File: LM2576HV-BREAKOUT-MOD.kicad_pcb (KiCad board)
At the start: 2 copper layers, 39 x 34 mm, 16 parts, among them J1 Conn_01x01, J2 Conn_01x01, J3 Conn_01x01, J4 Conn_01x01, U1 LM2576HVS-ADJ

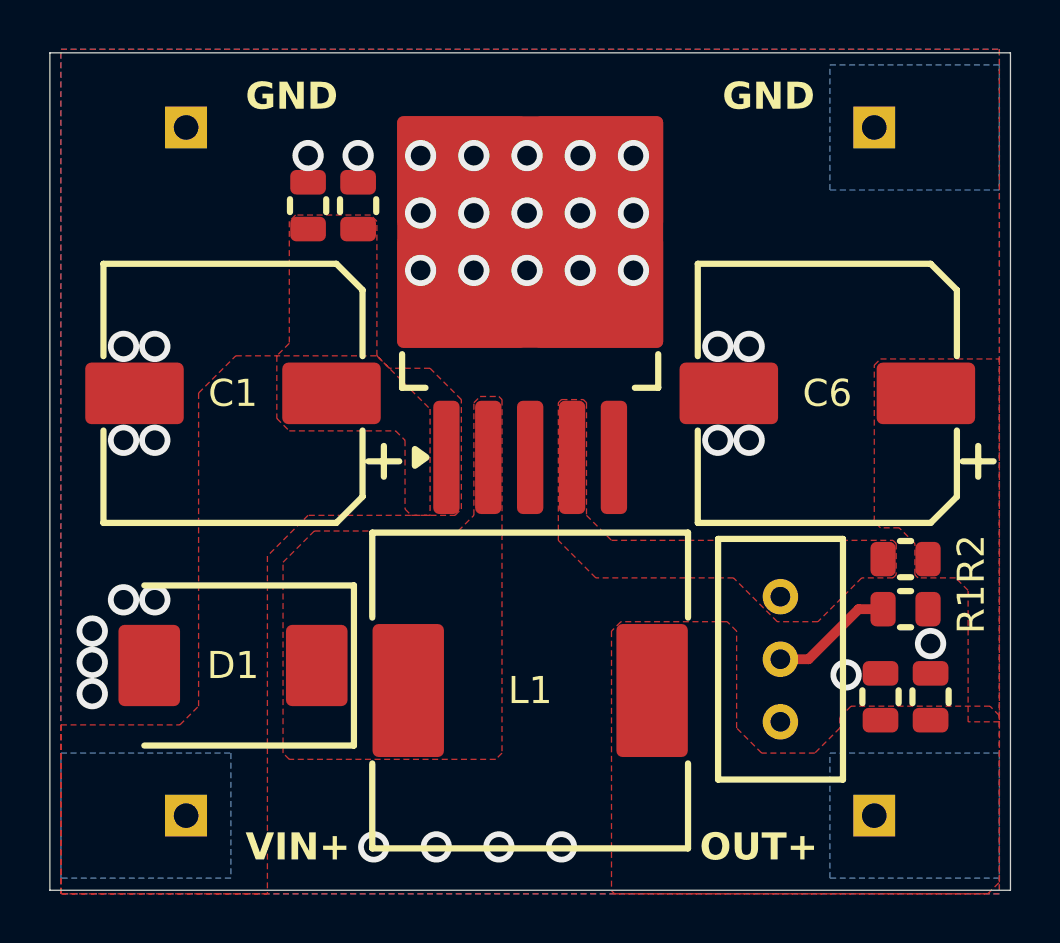
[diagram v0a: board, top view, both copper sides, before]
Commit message: Update LM2576HV Breakout Mod to use LM2576HVS-12
- Removed unused potentiometer symbol and associated properties from schematic.
- Updated LM2576HVS-ADJ references to LM2576HVS-12 in schematic, including properties and symbols.
- Adjusted junction and wire positions for better layout.
- Removed redundant wires and no-connects to clean up the schematic.
- Updated connector positions for better alignment.
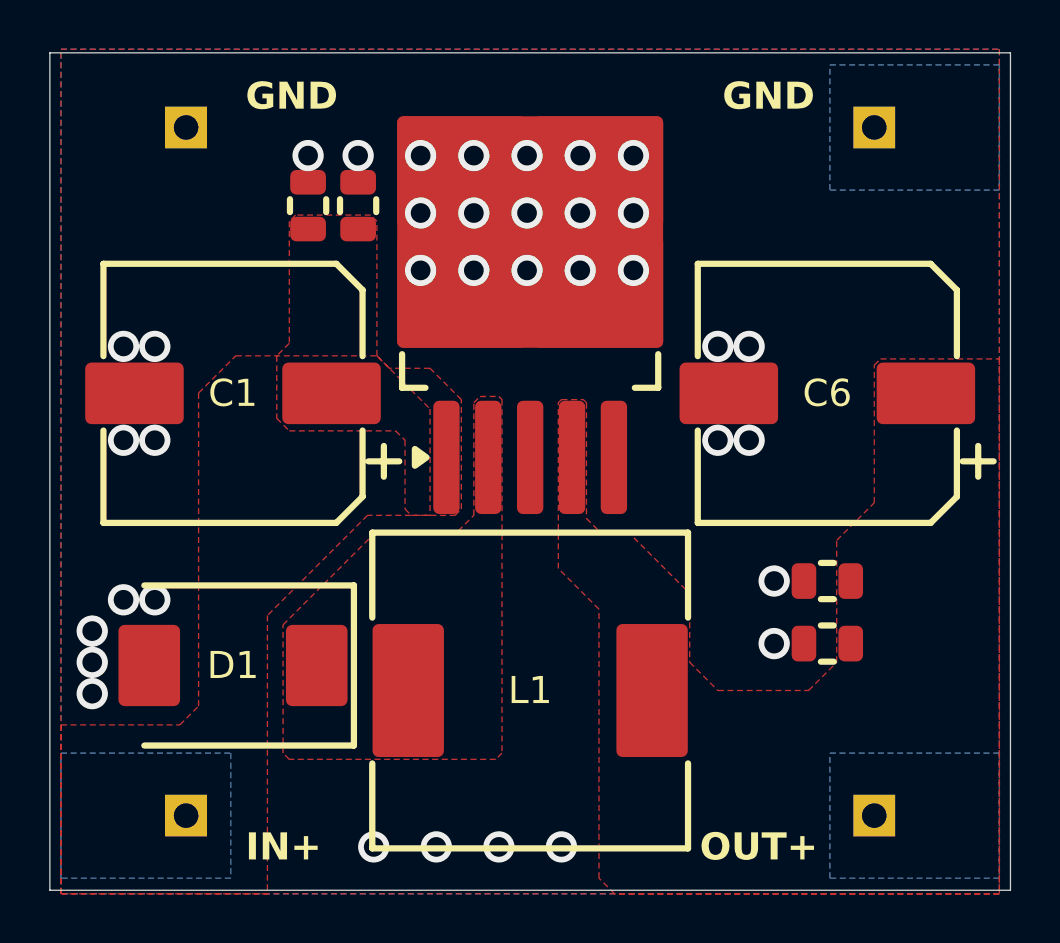
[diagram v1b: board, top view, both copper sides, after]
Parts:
- removed R1: 1k, Resistor_SMD:R_0805_2012Metric
- removed R2: 1k5, Resistor_SMD:R_0805_2012Metric
- removed RV1: 10k, Potentiometer_THT:Potentiometer_Bourns_3296W_Vertical
- U1: value LM2576HVS-ADJ -> LM2576HVS-12
- moved C4 6.30 mm to (177.2, 81.9), turned to 180 degrees
- moved C5 3.05 mm to (177.2, 84.5), turned to 180 degrees
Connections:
- U1 pad 4: FB -> VOUT
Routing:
- net /TRIM: track 5.01 -> 0.00 mm
- removed copper zone on F.Cu, net FB
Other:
- board text added: "IN+"
- board text removed: "VIN+"
